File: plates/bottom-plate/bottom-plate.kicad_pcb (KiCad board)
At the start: 2 copper layers, 140.5 x 112.5 mm, 0 parts

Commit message: added hybrid
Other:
- outline, holes or cut-outs redrawn

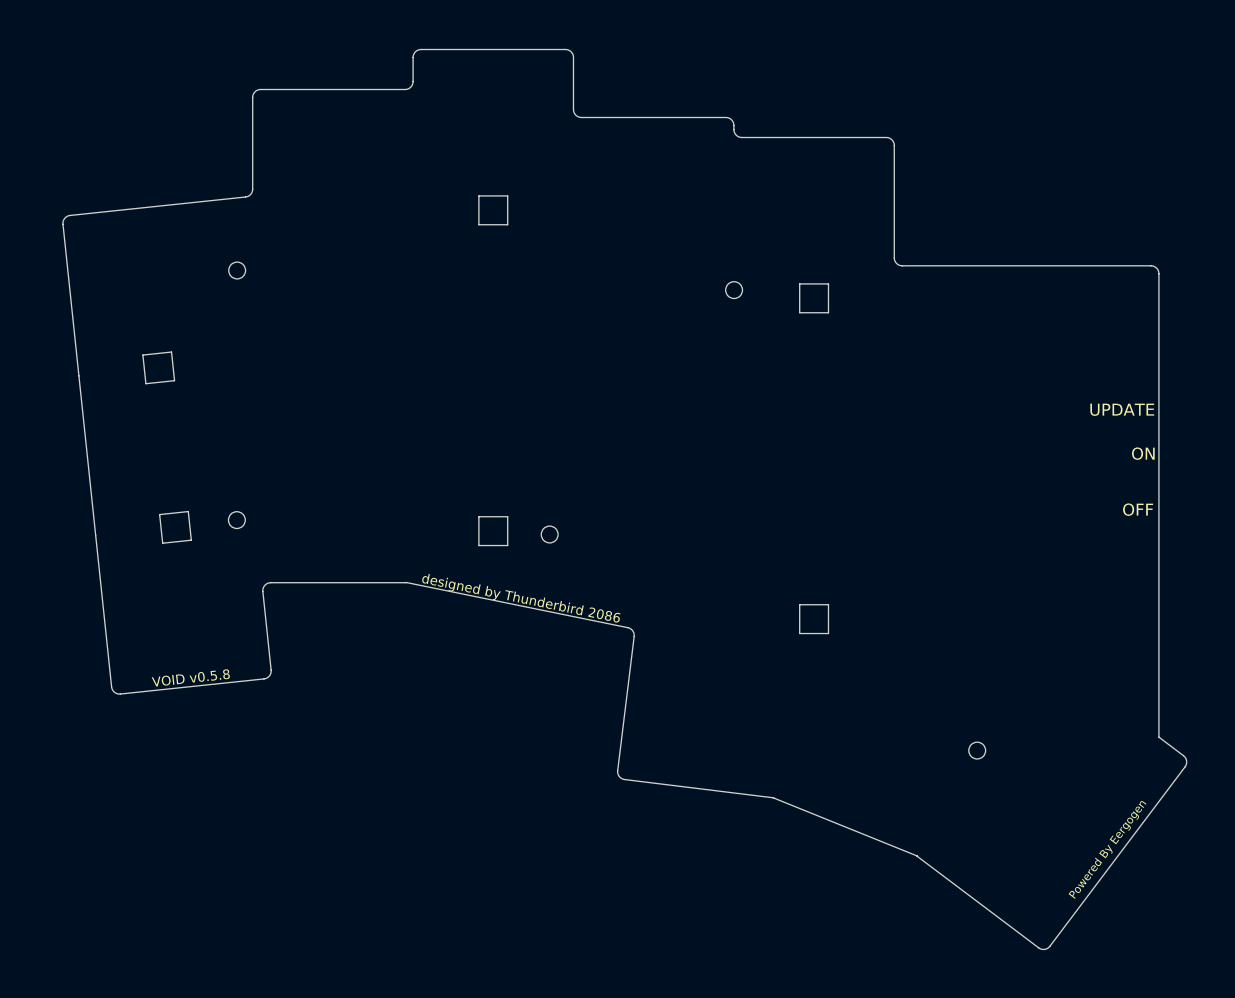
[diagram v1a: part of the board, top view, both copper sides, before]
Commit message: added choc
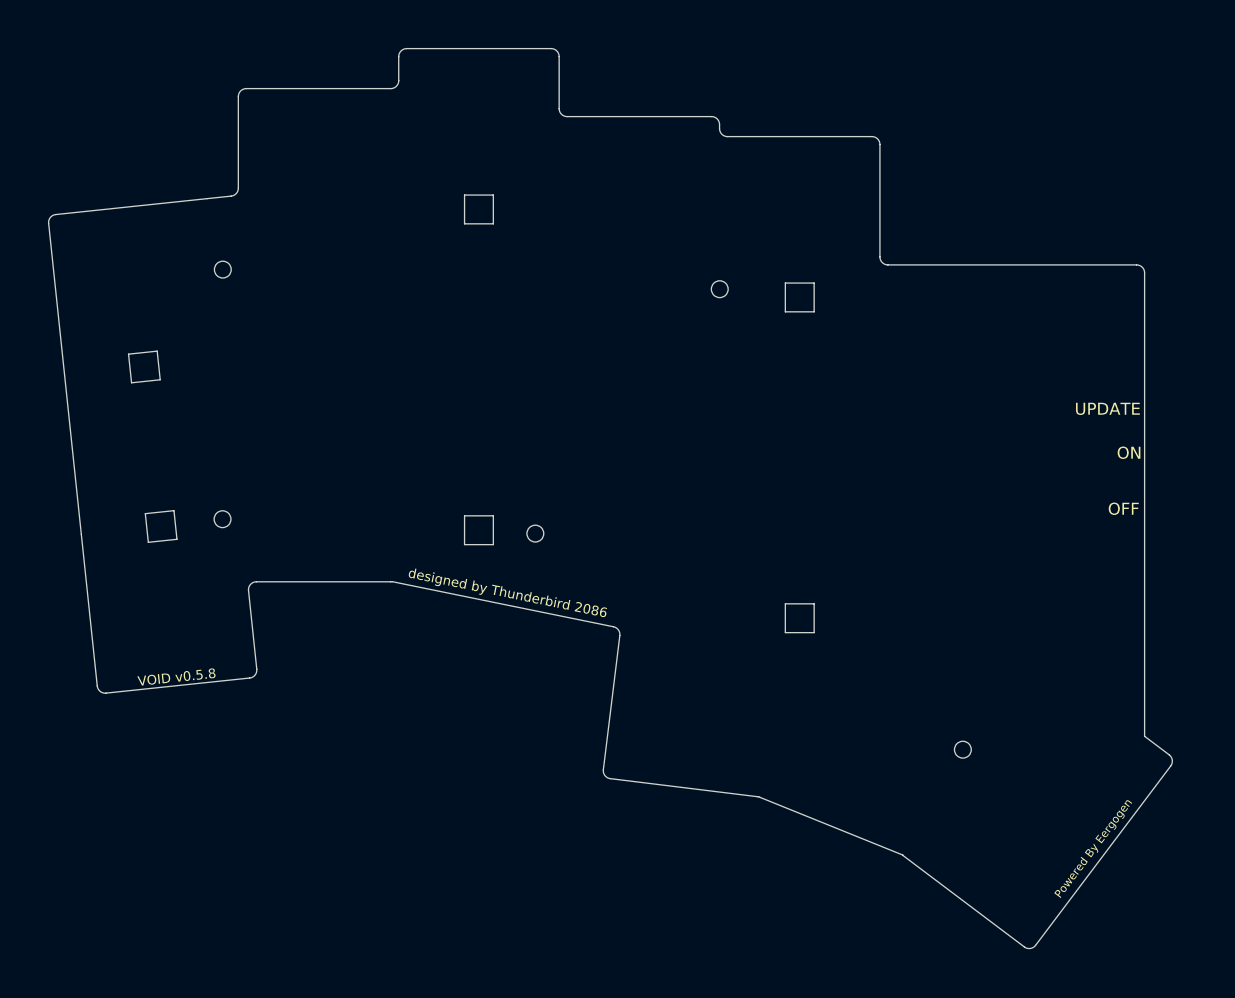
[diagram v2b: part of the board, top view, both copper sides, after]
